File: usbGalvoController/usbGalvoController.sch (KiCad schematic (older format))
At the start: 1 part

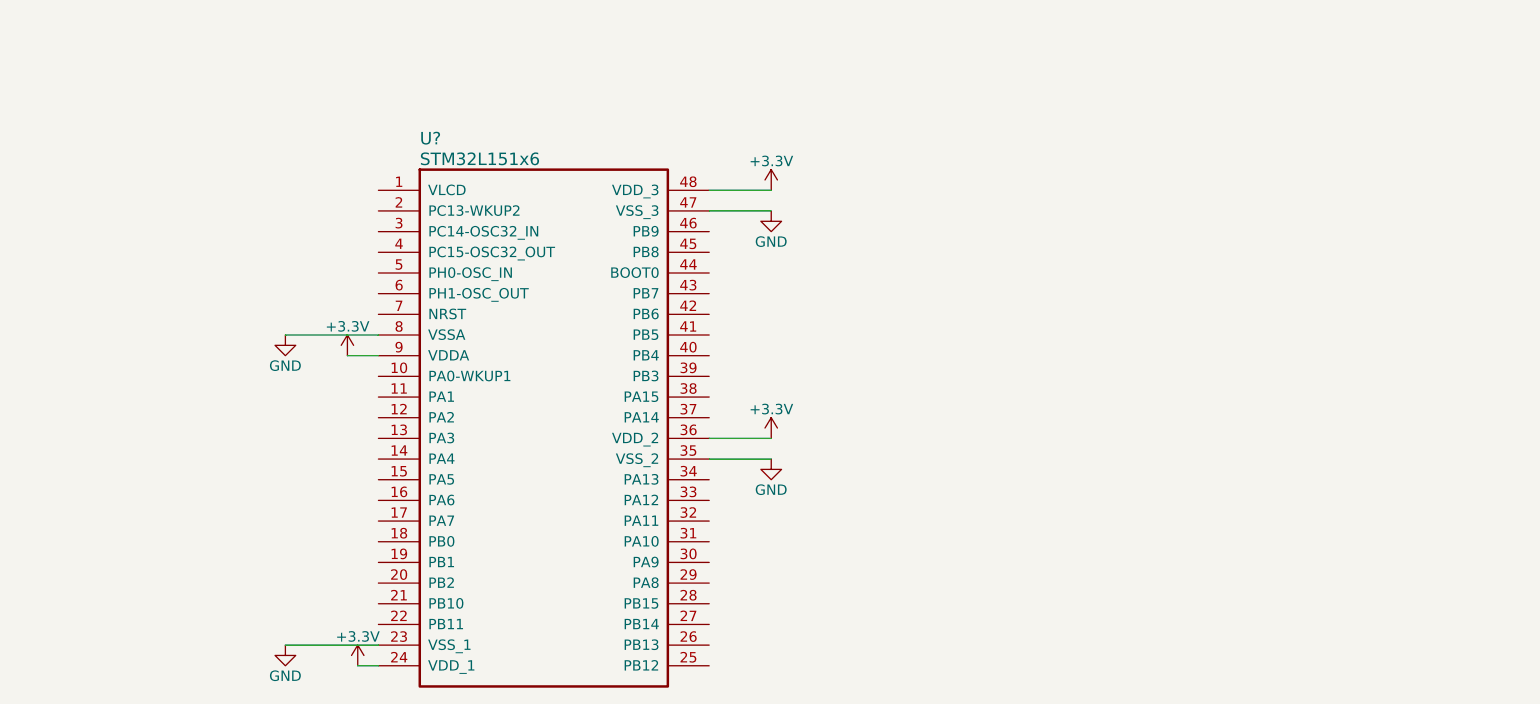
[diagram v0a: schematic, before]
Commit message: Added crystal and USB connections
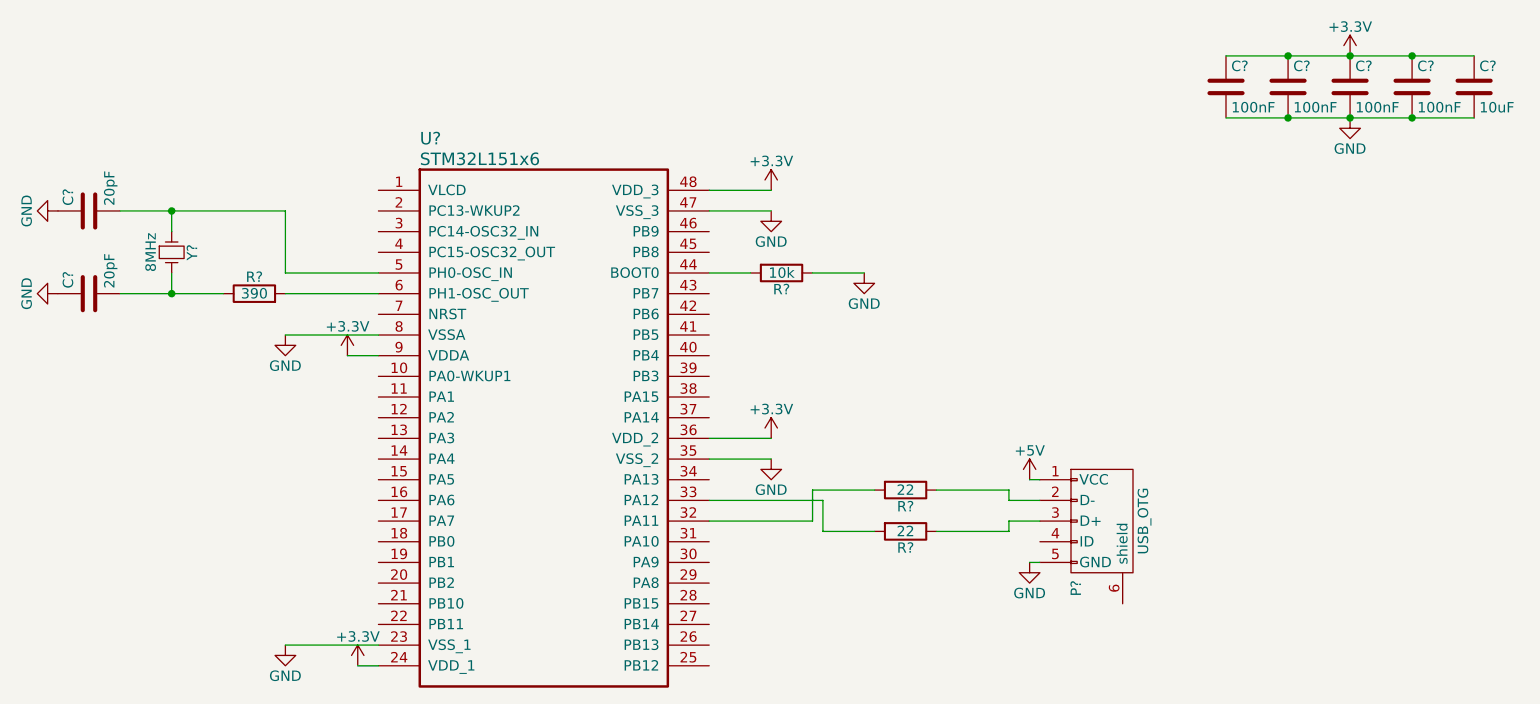
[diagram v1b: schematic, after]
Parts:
- added C? (x4): 100nF, symbol C
- added C?: 10uF, symbol C
- added C? (x2): 20pF, symbol C
- added P?: USB_OTG, symbol USB_OTG
- added R?: 390, symbol R
- added R?: 10k, symbol R
- added R? (x2): 22, symbol R
- added Y?: 8MHz, symbol Crystal_Small
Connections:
- net +3V3: now also C?.1, C?.1, C?.1, C?.1, C?.1
- net GND: now also C?.1, C?.1, C?.2, C?.2, C?.2, C?.2, C?.2, P?.5 (GND), R?.1
- net at U?.32 (PA11): now also R?.2
- net at U?.33 (PA12): now also R?.2
- net at U?.44 (BOOT0): now also R?.2
- net at U?.5 (PH0-OSC_IN): now also C?.2, Y?.1
- net at U?.6 (PH1-OSC_OUT): now also R?.2
- new net: C?.2, R?.1, Y?.2
- new net: P?.2 (D-), R?.1
- new net: P?.3 (D+), R?.1
- new net +5V: P?.1 (VCC)

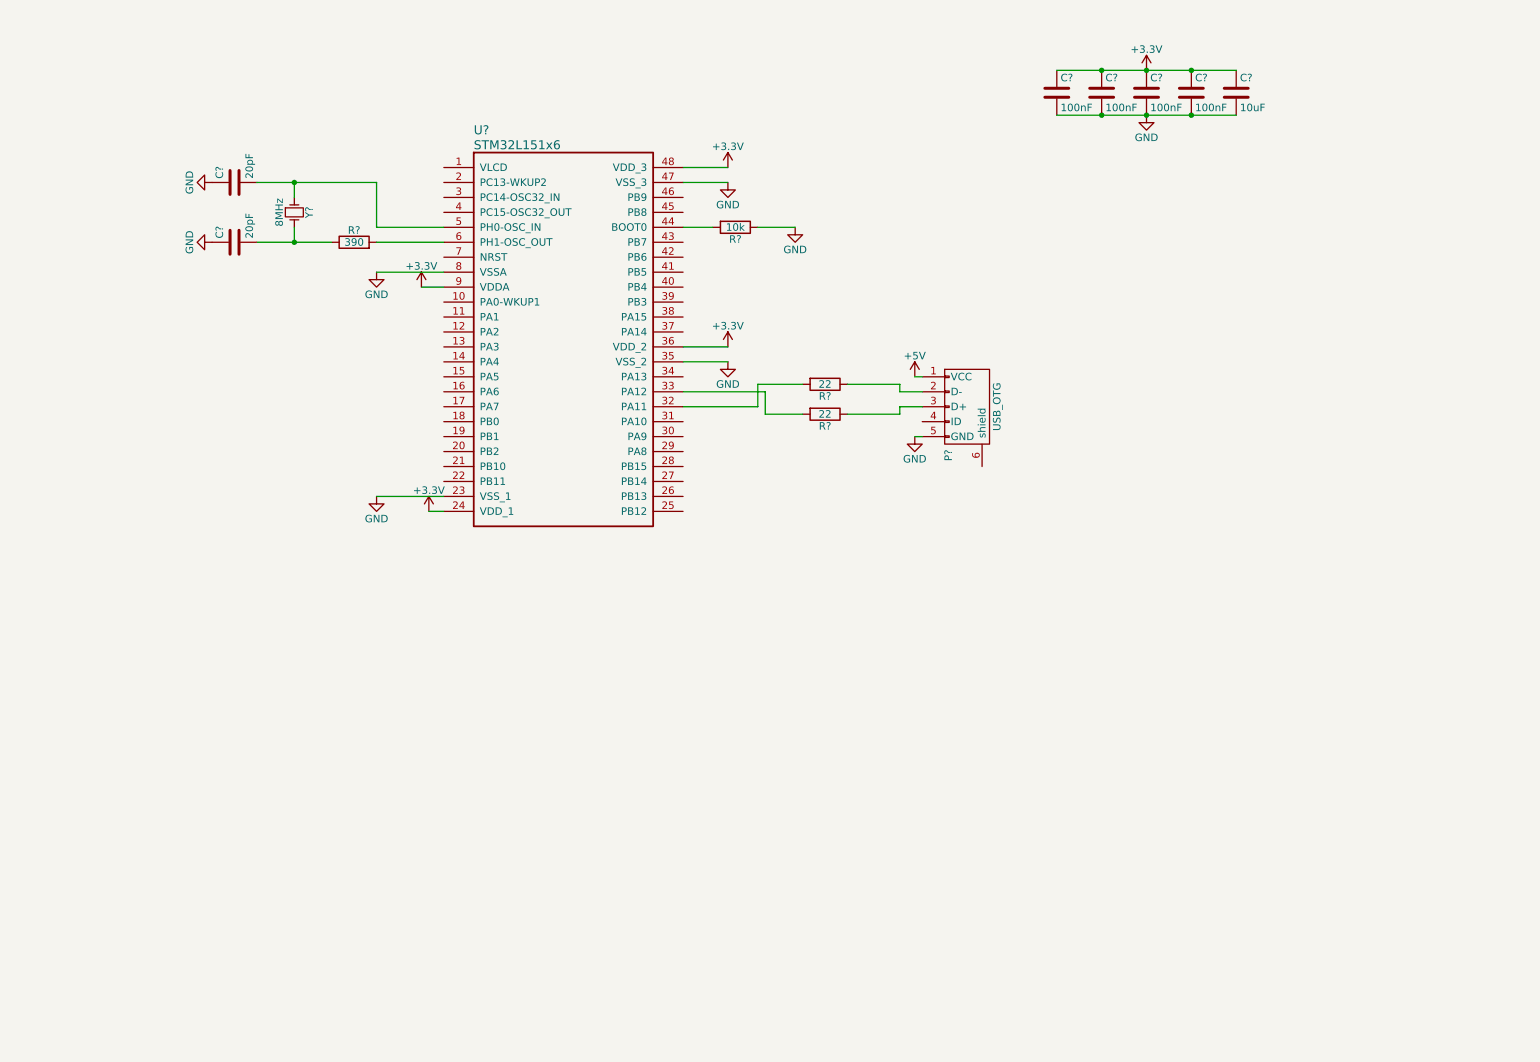
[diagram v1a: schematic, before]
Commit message: Schematic done for usbGalvoController (I think)
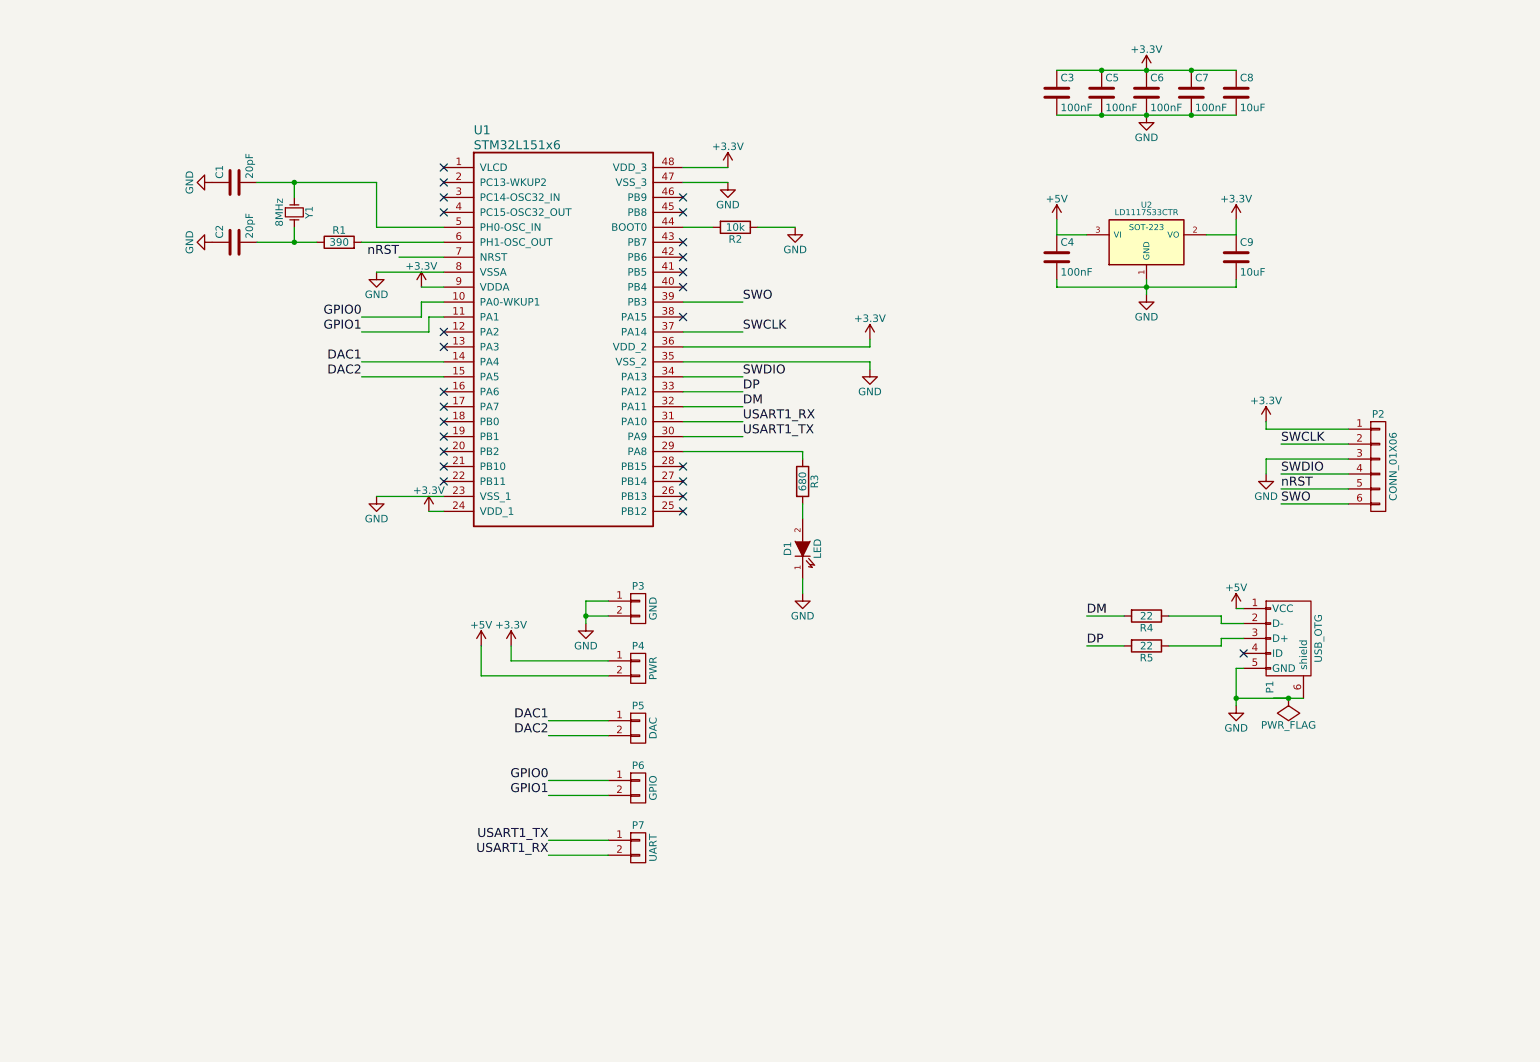
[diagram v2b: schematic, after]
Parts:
- added C4: 100nF, symbol C
- added C9: 10uF, symbol C
- added D1: LED, symbol LED
- added P2: CONN_01X06, symbol CONN_01X06
- added P3: GND, symbol CONN_01X02
- added P4: PWR, symbol CONN_01X02
- added P5: DAC, symbol CONN_01X02
- added P6: GPIO, symbol CONN_01X02
- added P7: UART, symbol CONN_01X02
- added R3: 680, symbol R
- added U2: LD1117S33CTR, SOT-223, symbol LD1117S33CTR
- gave numbers to parts that had none: 14
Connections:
- net +3V3: now also C9.1, P2.1 (P1), P4.1 (P1), U2.2 (VO)
- net +5V: now also C4.1, P4.2 (P2), U2.3 (VI)
- net GND: now also P1.6 (shield), C4.2, C9.2, D1.1 (K), P2.3 (P3), P3.1 (P1), P3.2 (P2), U2.1 (GND)
- net GPIO0: now reaches U1.10 (PA0-WKUP1)
- net GPIO0: now also P6.1 (P1)
- net GPIO1: now reaches U1.11 (PA1)
- net GPIO1: now also P6.2 (P2)
- net DAC1: now reaches U1.14 (PA4)
- net DAC1: now also P5.1 (P1)
- net DAC2: now reaches U1.15 (PA5)
- net DAC2: now also P5.2 (P2)
- net at U1.29 (PA8): now also R3.1
- net USART1_TX: now reaches U1.30 (PA9)
- net USART1_TX: now also P7.1 (P1)
- net USART1_RX: now reaches U1.31 (PA10)
- net USART1_RX: now also P7.2 (P2)
- net DM: now reaches R4.2, U1.32 (PA11)
- net DP: now reaches R5.2, U1.33 (PA12)
- net SWDIO: now reaches U1.34 (PA13)
- net SWDIO: now also P2.4 (P4)
- net SWCLK: now reaches U1.37 (PA14)
- net SWCLK: now also P2.2 (P2)
- net SWO: now reaches U1.39 (PB3)
- net SWO: now also P2.6 (P6)
- net nRST: now reaches U1.7 (NRST)
- net nRST: now also P2.5 (P5)
- new net: D1.2 (A), R3.2
- no-connect marks 0 -> 25
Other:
- moved on the sheet: P1, R1, R4, R5

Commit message: Layout done! (I think)
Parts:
- added R6: 1.5k, Resistors_SMD:R_0805, symbol R
- C1, C2, C3, C4, C5, C6, C7, C8, C9: footprint (none) -> Capacitors_SMD:C_0805
- D1: footprint (none) -> LEDs:LED-0805
- P1: footprint (none) -> alvarop:USB_MICRO_B
- P2: footprint (none) -> Pin_Headers:Pin_Header_Straight_1x06
- P3, P4, P5, P6, P7: footprint (none) -> Pin_Headers:Pin_Header_Straight_1x02
- R1, R2, R3, R4, R5: footprint (none) -> Resistors_SMD:R_0805
- U1: footprint (none) -> alvarop:LQFP48
- U2: footprint SOT-223 -> alvarop:SOT-223
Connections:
- net +3V3: now also R6.2
- net at U1.29 (PA8): no longer R3.1
- net at U1.38 (PA15): now also R3.1
- net at P1.3 (D+), R5.1: now also R6.1
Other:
- moved on the sheet: D1, R3
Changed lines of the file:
@@
 LIBS:valves
 LIBS:STM32L151x6
+LIBS:usbGalvoController-cache
 EELAYER 25 0
 EELAYER END
@@
 F 0 "U1" H 4000 1900 60  0000 L CNN
 F 1 "STM32L151x6" H 4000 1800 60  0000 L CNN
-F 2 "" H 3800 1650 60  0000 C CNN
+F 2 "alvarop:LQFP48" H 3800 1650 60  0001 C CNN
 F 3 "" H 3800 1650 60  0000 C CNN
 	1    3800 1650
@@
 F 0 "C3" H 7925 1250 50  0000 L CNN
 F 1 "100nF" H 7925 1050 50  0000 L CNN
-F 2 "" H 7938 1000 30  0000 C CNN
+F 2 "Capacitors_SMD:C_0805" H 7938 1000 30  0001 C CNN
 F 3 "" H 7900 1150 60  0000 C CNN
 	1    7900 1150
@@
 F 0 "C6" H 8525 1250 50  0000 L CNN
 F 1 "100nF" H 8525 1050 50  0000 L CNN
-F 2 "" H 8538 1000 30  0000 C CNN
+F 2 "Capacitors_SMD:C_0805" H 8538 1000 30  0001 C CNN
 F 3 "" H 8500 1150 60  0000 C CNN
 	1    8500 1150
@@
 F 0 "C7" H 8825 1250 50  0000 L CNN
 F 1 "100nF" H 8825 1050 50  0000 L CNN
-F 2 "" H 8838 1000 30  0000 C CNN
+F 2 "Capacitors_SMD:C_0805" H 8838 1000 30  0001 C CNN
 F 3 "" H 8800 1150 60  0000 C CNN
 	1    8800 1150
@@
 F 0 "C8" H 9125 1250 50  0000 L CNN
 F 1 "10uF" H 9125 1050 50  0000 L CNN
-F 2 "" H 9138 1000 30  0000 C CNN
+F 2 "Capacitors_SMD:C_0805" H 9138 1000 30  0001 C CNN
 F 3 "" H 9100 1150 60  0000 C CNN
 	1    9100 1150
@@
 F 0 "C5" H 8225 1250 50  0000 L CNN
 F 1 "100nF" H 8225 1050 50  0000 L CNN
-F 2 "" H 8238 1000 30  0000 C CNN
+F 2 "Capacitors_SMD:C_0805" H 8238 1000 30  0001 C CNN
 F 3 "" H 8200 1150 60  0000 C CNN
 	1    8200 1150
@@
 F 0 "C1" H 2425 1850 50  0000 L CNN
 F 1 "20pF" H 2425 1650 50  0000 L CNN
-F 2 "" H 2438 1600 30  0000 C CNN
+F 2 "Capacitors_SMD:C_0805" H 2438 1600 30  0001 C CNN
 F 3 "" H 2400 1750 60  0000 C CNN
 	1    2400 1750
@@
 F 0 "C2" H 2425 2250 50  0000 L CNN
 F 1 "20pF" H 2425 2050 50  0000 L CNN
-F 2 "" H 2438 2000 30  0000 C CNN
+F 2 "Capacitors_SMD:C_0805" H 2438 2000 30  0001 C CNN
 F 3 "" H 2400 2150 60  0000 C CNN
 	1    2400 2150
@@
 F 0 "Y1" H 2800 2050 50  0000 C CNN
 F 1 "8MHz" H 2800 1850 50  0000 C CNN
-F 2 "" H 2800 1950 60  0000 C CNN
+F 2 "" H 2800 1950 60  0001 C CNN
 F 3 "" H 2800 1950 60  0000 C CNN
 	1    2800 1950
@@
 F 0 "R1" V 3180 2150 50  0000 C CNN
 F 1 "390" V 3100 2150 50  0000 C CNN
-F 2 "" V 3030 2150 30  0000 C CNN
+F 2 "Resistors_SMD:R_0805" V 3030 2150 30  0001 C CNN
 F 3 "" H 3100 2150 30  0000 C CNN
 	1    3100 2150
@@
 F 0 "R2" V 5830 2050 50  0000 C CNN
 F 1 "10k" V 5750 2050 50  0000 C CNN
-F 2 "" V 5680 2050 30  0000 C CNN
+F 2 "Resistors_SMD:R_0805" V 5680 2050 30  0001 C CNN
 F 3 "" H 5750 2050 30  0000 C CNN
 	1    5750 2050
@@
 F 0 "P1" H 9775 4675 50  0000 C CNN
 F 1 "USB_OTG" H 9450 5000 50  0000 C CNN
-F 2 "" V 9400 4700 60  0000 C CNN
+F 2 "alvarop:USB_MICRO_B" V 9400 4700 60  0001 C CNN
 F 3 "" V 9400 4700 60  0000 C CNN
 	1    9450 4800
@@
 F 0 "R4" V 8580 4650 50  0000 C CNN
 F 1 "22" V 8500 4650 50  0000 C CNN
-F 2 "" V 8430 4650 30  0000 C CNN
+F 2 "Resistors_SMD:R_0805" V 8430 4650 30  0001 C CNN
 F 3 "" H 8500 4650 30  0000 C CNN
 	1    8500 4650
@@
 F 0 "R5" V 8580 4850 50  0000 C CNN
 F 1 "22" V 8500 4850 50  0000 C CNN
-F 2 "" V 8430 4850 30  0000 C CNN
+F 2 "Resistors_SMD:R_0805" V 8430 4850 30  0001 C CNN
 F 3 "" H 8500 4850 30  0000 C CNN
 	1    8500 4850
@@
 F 0 "U2" H 8500 2400 40  0000 C CNN
 F 1 "LD1117S33CTR" H 8500 2350 40  0000 C CNN
-F 2 "SOT-223" H 8500 2250 40  0000 C CNN
+F 2 "alvarop:SOT-223" H 8500 2250 40  0001 C CNN
 F 3 "" H 8500 2150 60  0000 C CNN
 	1    8500 2150
@@
 F 0 "C4" H 7925 2350 50  0000 L CNN
 F 1 "100nF" H 7925 2150 50  0000 L CNN
-F 2 "" H 7938 2100 30  0000 C CNN
+F 2 "Capacitors_SMD:C_0805" H 7938 2100 30  0001 C CNN
 F 3 "" H 7900 2250 60  0000 C CNN
 	1    7900 2250
@@
 F 0 "C9" H 9125 2350 50  0000 L CNN
 F 1 "10uF" H 9125 2150 50  0000 L CNN
-F 2 "" H 9138 2100 30  0000 C CNN
+F 2 "Capacitors_SMD:C_0805" H 9138 2100 30  0001 C CNN
 F 3 "" H 9100 2250 60  0000 C CNN
 	1    9100 2250
@@
 F 0 "P2" H 10050 4000 50  0000 C CNN
 F 1 "CONN_01X06" V 10150 3650 50  0000 C CNN
-F 2 "" H 10050 3650 60  0000 C CNN
+F 2 "Pin_Headers:Pin_Header_Straight_1x06" H 10050 3650 60  0001 C CNN
 F 3 "" H 10050 3650 60  0000 C CNN
 	1    10050 3650
@@
 L LED D1
 U 1 1 5606F018
-P 6200 4200
-F 0 "D1" H 6200 4300 50  0000 C CNN
-F 1 "LED" H 6200 4100 50  0000 C CNN
-F 2 "" H 6200 4200 60  0000 C CNN
-F 3 "" H 6200 4200 60  0000 C CNN
-	1    6200 4200
+P 7100 3250
+F 0 "D1" H 7100 3350 50  0000 C CNN
+F 1 "LED" H 7100 3150 50  0000 C CNN
+F 2 "LEDs:LED-0805" H 7100 3250 60  0001 C CNN
+F 3 "" H 7100 3250 60  0000 C CNN
+	1    7100 3250
 	0    -1   -1   0
 $EndComp
@@
 L R R3
 U 1 1 5606F0F5
-P 6200 3750
-F 0 "R3" V 6280 3750 50  0000 C CNN
-F 1 "680" V 6200 3750 50  0000 C CNN
-F 2 "" V 6130 3750 30  0000 C CNN
-F 3 "" H 6200 3750 30  0000 C CNN
-	1    6200 3750
+P 7100 2800
+F 0 "R3" V 7180 2800 50  0000 C CNN
+F 1 "680" V 7100 2800 50  0000 C CNN
+F 2 "Resistors_SMD:R_0805" V 7030 2800 30  0001 C CNN
+F 3 "" H 7100 2800 30  0000 C CNN
+	1    7100 2800
 	1    0    0    -1
 $EndComp
@@
 L GND #PWR021
 U 1 1 5606F15F
-P 6200 4500
-F 0 "#PWR021" H 6200 4250 50  0001 C CNN
-F 1 "GND" H 6200 4350 50  0000 C CNN
-F 2 "" H 6200 4500 60  0000 C CNN
-F 3 "" H 6200 4500 60  0000 C CNN
-	1    6200 4500
-	1    0    0    -1
-$EndComp
-Wire Wire Line
-	6200 4500 6200 4400
-Wire Wire Line
-	6200 4000 6200 3900
-Wire Wire Line
-	5400 3550 6200 3550
-Wire Wire Line
-	6200 3550 6200 3600
+P 7100 3550
+F 0 "#PWR021" H 7100 3300 50  0001 C CNN
+F 1 "GND" H 7100 3400 50  0000 C CNN
+F 2 "" H 7100 3550 60  0000 C CNN
+F 3 "" H 7100 3550 60  0000 C CNN
+	1    7100 3550
+	1    0    0    -1
+$EndComp
+Wire Wire Line
+	7100 3550 7100 3450
+Wire Wire Line
+	7100 3050 7100 2950
+Wire Wire Line
+	7100 2550 7100 2650
 Text Label 3250 2650 2    60   ~ 0
 GPIO0
@@
 NoConn ~ 5400 3750
 NoConn ~ 5400 3650
-NoConn ~ 5400 2650
 NoConn ~ 5400 2450
 NoConn ~ 5400 2350
@@
 F 0 "P4" H 5100 5150 50  0000 C CNN
 F 1 "PWR" V 5200 5000 50  0000 C CNN
-F 2 "" H 5100 5000 60  0000 C CNN
+F 2 "Pin_Headers:Pin_Header_Straight_1x02" H 5100 5000 60  0001 C CNN
 F 3 "" H 5100 5000 60  0000 C CNN
 	1    5100 5000
@@
 F 0 "P5" H 5100 5550 50  0000 C CNN
 F 1 "DAC" V 5200 5400 50  0000 C CNN
-F 2 "" H 5100 5400 60  0000 C CNN
+F 2 "Pin_Headers:Pin_Header_Straight_1x02" H 5100 5400 60  0001 C CNN
 F 3 "" H 5100 5400 60  0000 C CNN
 	1    5100 5400
@@
 F 0 "P6" H 5100 5950 50  0000 C CNN
 F 1 "GPIO" V 5200 5800 50  0000 C CNN
-F 2 "" H 5100 5800 60  0000 C CNN
+F 2 "Pin_Headers:Pin_Header_Straight_1x02" H 5100 5800 60  0001 C CNN
 F 3 "" H 5100 5800 60  0000 C CNN
 	1    5100 5800
@@
 F 0 "P3" H 5100 4750 50  0000 C CNN
 F 1 "GND" V 5200 4600 50  0000 C CNN
-F 2 "" H 5100 4600 60  0000 C CNN
+F 2 "Pin_Headers:Pin_Header_Straight_1x02" H 5100 4600 60  0001 C CNN
 F 3 "" H 5100 4600 60  0000 C CNN
 	1    5100 4600
@@
 F 0 "P7" H 5100 6350 50  0000 C CNN
 F 1 "UART" V 5200 6200 50  0000 C CNN
-F 2 "" H 5100 6200 60  0000 C CNN
+F 2 "Pin_Headers:Pin_Header_Straight_1x02" H 5100 6200 60  0001 C CNN
 F 3 "" H 5100 6200 60  0000 C CNN
 	1    5100 6200
@@
 	9450 5200 9350 5200
 Connection ~ 9450 5200
+$Comp
+L R R6
+U 1 1 56071782
+P 8500 5100
+F 0 "R6" V 8580 5100 50  0000 C CNN
+F 1 "1.5k" V 8500 5100 50  0000 C CNN
+F 2 "Resistors_SMD:R_0805" V 8430 5100 30  0001 C CNN
+F 3 "" H 8500 5100 30  0000 C CNN
+	1    8500 5100
+	0    1    1    0
+$EndComp
+Wire Wire Line
+	8650 5100 8750 5100
+Wire Wire Line
+	8750 5100 8750 4850
+Connection ~ 8750 4850
+Wire Wire Line
+	8350 5100 7950 5100
+Wire Wire Line
+	7950 5100 7950 5000
+$Comp
+L +3.3V #PWR026
+U 1 1 560719AB
+P 7950 5000
+F 0 "#PWR026" H 7950 4850 50  0001 C CNN
+F 1 "+3.3V" H 7950 5140 50  0000 C CNN
+F 2 "" H 7950 5000 60  0000 C CNN
+F 3 "" H 7950 5000 60  0000 C CNN
+	1    7950 5000
+	1    0    0    -1
+$EndComp
+Wire Wire Line
+	5400 2650 6400 2650
+Wire Wire Line
+	6400 2650 6400 2550
+Wire Wire Line
+	6400 2550 7100 2550
+NoConn ~ 5400 3550
 $EndSCHEMATC
